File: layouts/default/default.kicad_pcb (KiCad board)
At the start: 2 copper layers, 37 x 37 mm, 109 parts

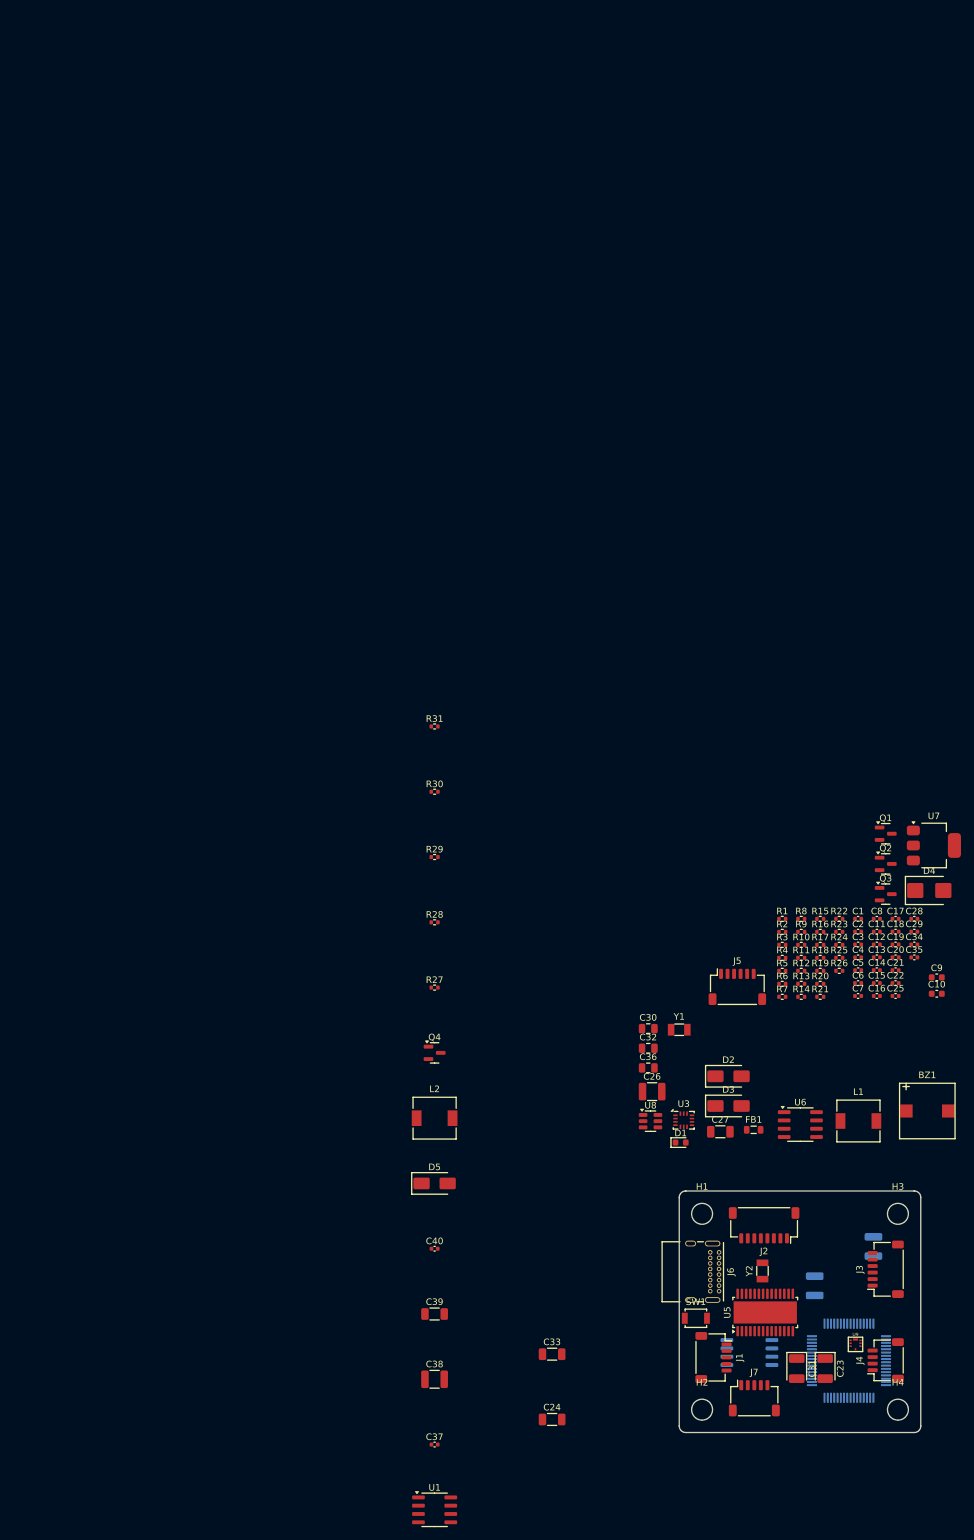
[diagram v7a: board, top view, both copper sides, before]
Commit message: REV-009: Replace MP1584EN with TI LMR43620 for NDAA compliance
Switch both buck converters from MPS MP1584EN (SOIC-8, asynchronous) to
TI LMR43620 (VQFN-HR 2x2mm, synchronous, internally compensated).
5V BEC uses fixed-output LMR43620MB5RPER; 10V VTX BEC uses adjustable
LMR43620RNXTRPER with 90.9k/10k FB divider (VREF=1.0V).

Removes external Schottky catch diodes, compensation networks, and 5V
feedback divider. Adds VCC bypass caps, VIN HF bypass caps, and custom
13-pad VQFN-HR footprint with L-shaped corner pads.

Co-Authored-By: Claude Opus 4.6 <noreply@anthropic.com>
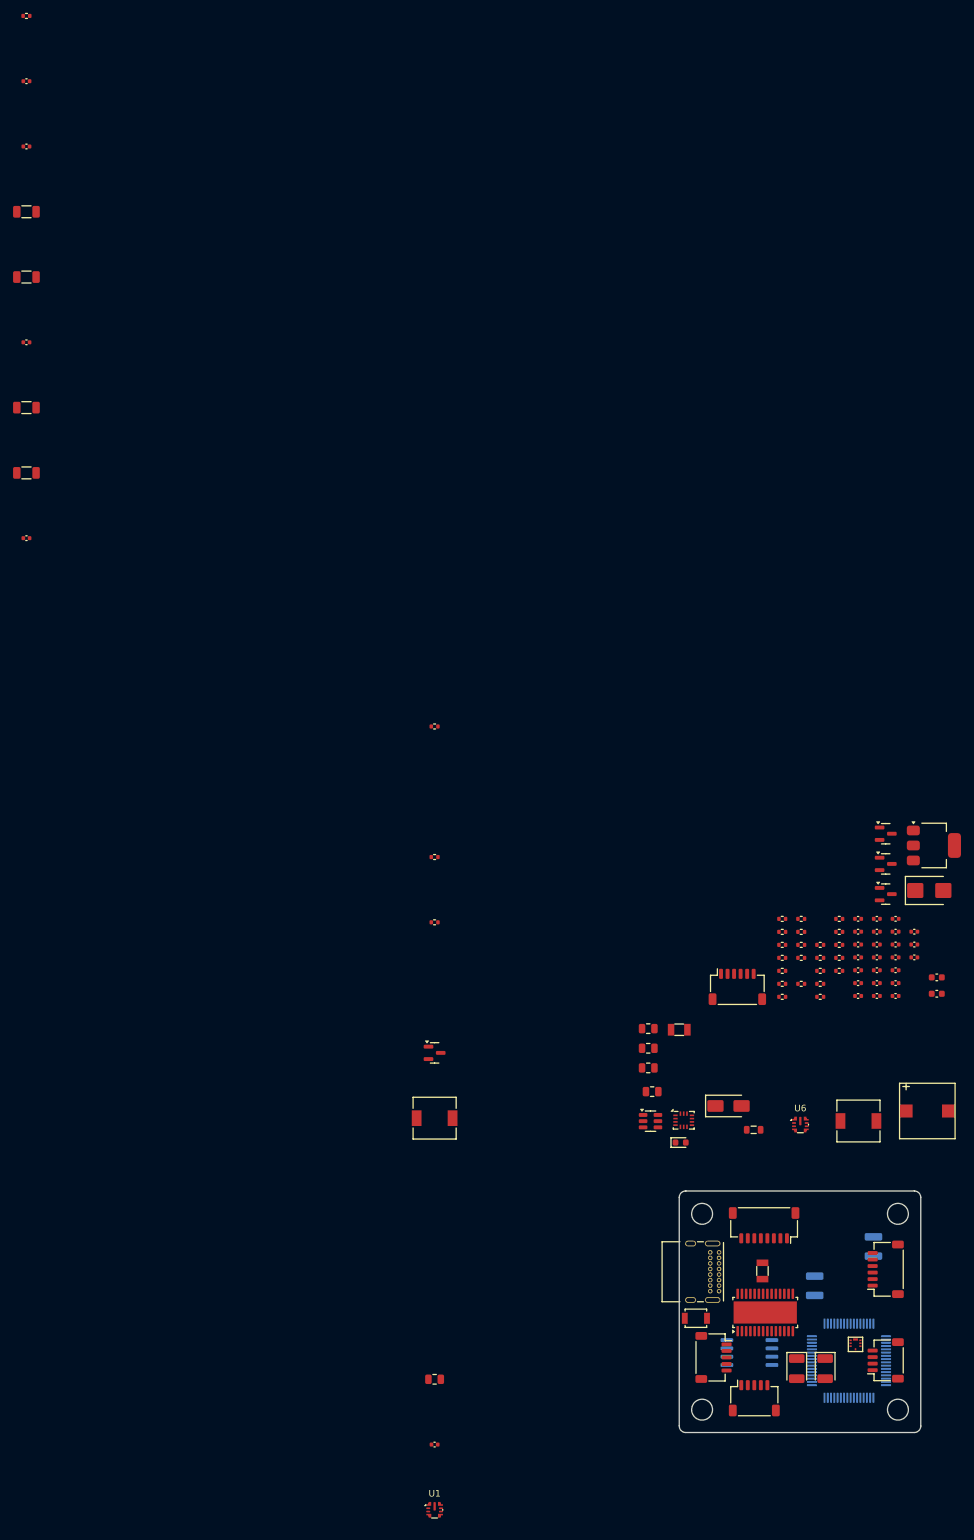
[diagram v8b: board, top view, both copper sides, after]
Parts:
- removed D2, D5: , Diode_SMD:D_SMA
- removed R14, R15, R16, R27, R30: , Resistor_SMD:R_0402_1005Metric
- added C43: , Capacitor_SMD:C_0402_1005Metric, F.Cu at (0.00, -60.0)
- added C44: , Capacitor_SMD:C_0402_1005Metric, F.Cu at (0.00, -70.0)
- C24, C33: footprint Capacitor_SMD:C_1206_3216Metric -> Capacitor_SMD:C_0402_1005Metric
- C26, C38: footprint Capacitor_SMD:C_1210_3225Metric -> Capacitor_SMD:C_0805_2012Metric
- C28, C40: footprint Capacitor_SMD:C_0402_1005Metric -> Capacitor_SMD:C_1206_3216Metric
- U1, U6: value (none) -> TI_RPE0009B_VQFN-HR-9_2x2mm_P0.5mm; footprint Package_SO:SOIC-8_3.9x4.9mm_P1.27mm -> lib:TI_RPE0009B_VQFN-HR-9_2x2mm_P0.5mm
- moved R12 188.4 mm to (0.00, -80.0)
- moved C33 174.7 mm to (0.00, -30.0)
- moved C39 170.7 mm to (0.00, -40.0)
- moved C40 170.7 mm to (0.00, -50.0)
- moved C24 157.2 mm to (0.00, 0.00)
- moved C28 156.9 mm to (0.00, -20.0)
- moved C27 146.6 mm to (0.00, -10.0)
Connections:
- C24 pad 1: v5 -> vbat
- C25 pad 1: buck-bst -> buck-boot
- C25 pad 2: buck-cathode -> buck-sw
- C27 pad 1: v5 -> rail_10v
- C28 pad 1: c_comp-_1 -> rail_10v
- C33 pad 1: v5 -> vbat
- C37 pad 1: buck_10v-bst -> buck_10v-boot
- C37 pad 2: buck_10v-cathode -> buck_10v-sw
- C39 pad 1: rail_10v -> v5
- C40 pad 1: c_comp_10v-_1 -> v5
- L1 pad 1: buck-cathode -> buck-sw
- L2 pad 1: buck_10v-cathode -> buck_10v-sw
- R12 pad 1: buck-comp -> rt
- R12 pad 2: c_comp-_1 -> baro-gnd
- R28 pad 1: buck_10v-fb -> fb
- R29 pad 2: buck_10v-fb -> fb
- U1 pad 1: buck_10v-cathode -> rt
- U1 pad 2: vbat -> buck_10v-pgood
- U1 pad 3: buck_10v-comp -> vbat
- U1 pad 4: buck_10v-fb -> vbat
- U1 pad 5: baro-gnd -> buck_10v-sw
- U1 pad 6: buck_10v-freq -> buck_10v-boot
- U1 pad 7: vbat -> buck_10v-vcc
- U1 pad 8: buck_10v-bst -> fb
- U6 pad 1: buck-cathode -> baro-gnd
- U6 pad 2: vbat -> buck-pgood
- U6 pad 3: buck-comp -> vbat
- U6 pad 4: buck-fb -> vbat
- U6 pad 5: baro-gnd -> buck-sw
- U6 pad 6: buck-freq -> buck-boot
- U6 pad 7: vbat -> buck-vcc
- U6 pad 8: buck-bst -> v5
